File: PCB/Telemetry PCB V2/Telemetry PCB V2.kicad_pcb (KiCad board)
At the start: 4 copper layers, 70 x 70 mm, 44 parts, among them IC1 E22-900M22S, J1 USB_C_Receptacle_USB2.0_16P, J2 Batt, J3 Serial Debug Header 1x4, J4 GPS, J5 Conn_01x04_Pin, SW1 SW_MEC_5E, SW2 SW_MEC_5E, U1 AP62200WU, U2 STM32F411CEUx, U3 MCP1700x-250xxTT, Y1 25MHZ 20pF, Y2 32.768k 12.5pF

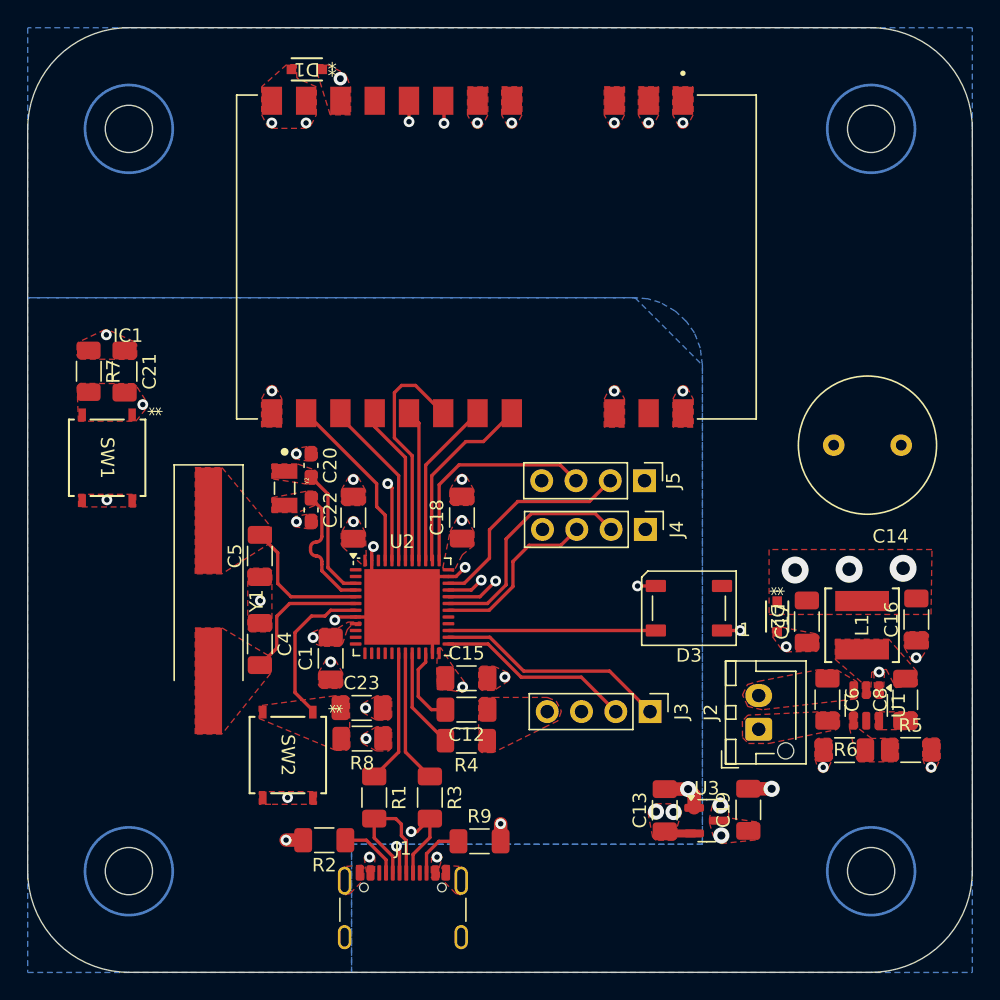
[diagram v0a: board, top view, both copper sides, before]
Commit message: Changed lines around holes to ruled zones
the lines that were used to prevent fills were becoming traces so I changed them to rule zones that prevent anything from entering the zone
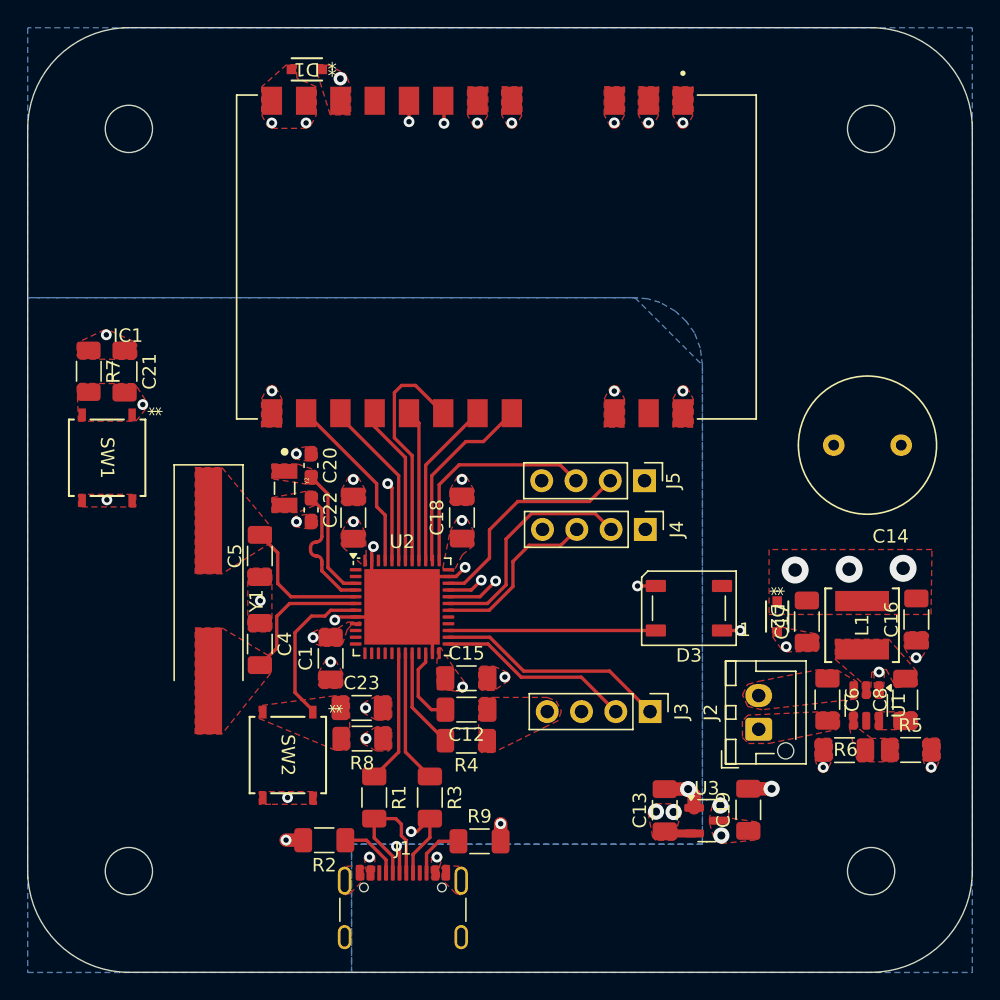
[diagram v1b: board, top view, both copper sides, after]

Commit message: changed many things
changed capacitor footprint, moved tx2 and rx2 to a uart pin. moved nrst switch moved j3 header
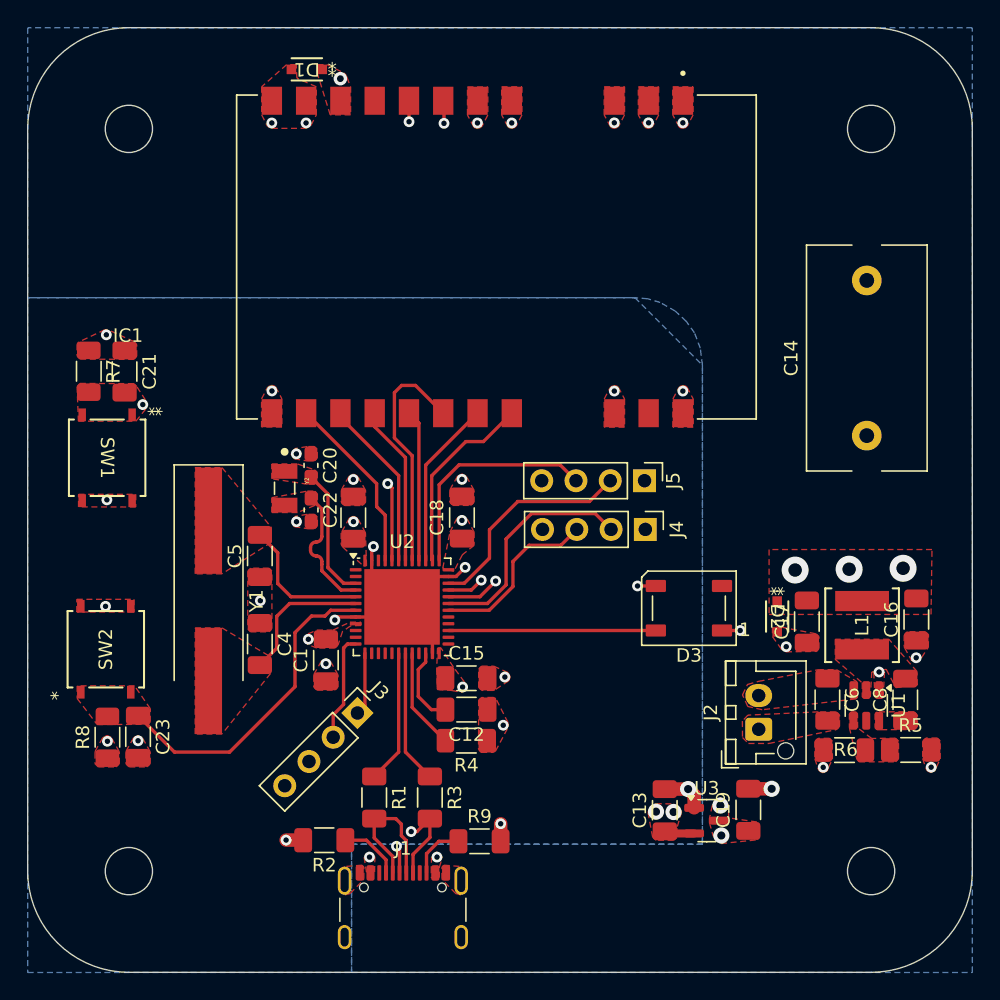
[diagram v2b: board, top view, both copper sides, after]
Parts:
- C14: footprint Capacitor_THT:C_Radial_D10.0mm_H20.0mm_P5.00mm -> PLZ5V1C_G3_H:C_Rect_L16.5mm_W8.7mm_P11.50mm_MKT
- moved J3 21.7 mm to (147.3, 99.2), turned to -45 degrees
- moved R8 18.9 mm to (128.8, 101.0), turned to 90 degrees
- moved C23 16.7 mm to (131.1, 101.0), turned to -90 degrees
- moved SW2 15.6 mm to (128.7, 94.5), turned to 90 degrees
- moved C14 2.76 mm to (185.1, 80.4), turned to 90 degrees
- moved C1 0.37 mm to (145.0, 95.3)
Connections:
- U2 pad 12: unconnected-(U2-PA2-Pad12) -> TX2
- U2 pad 13: unconnected-(U2-PA3-Pad13) -> RX2
- U2 pad 25: TX2 -> unconnected-(U2-PB12-Pad25)
- U2 pad 26: RX2 -> unconnected-(U2-PB13-Pad26)
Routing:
- net RX2: track 17.2 -> 4.66 mm
- net NRST: track 11.6 -> 23.9 mm
- net TX2: track 14.5 -> 7.95 mm
- net GND: vias 32 -> 33

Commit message: Revamped power, made usb better
Revamped the layout of the voltage regulator to match closer to the recommend layout form the data sheet.
Realized I didn't need vias for the usb lines so they are much nicer now
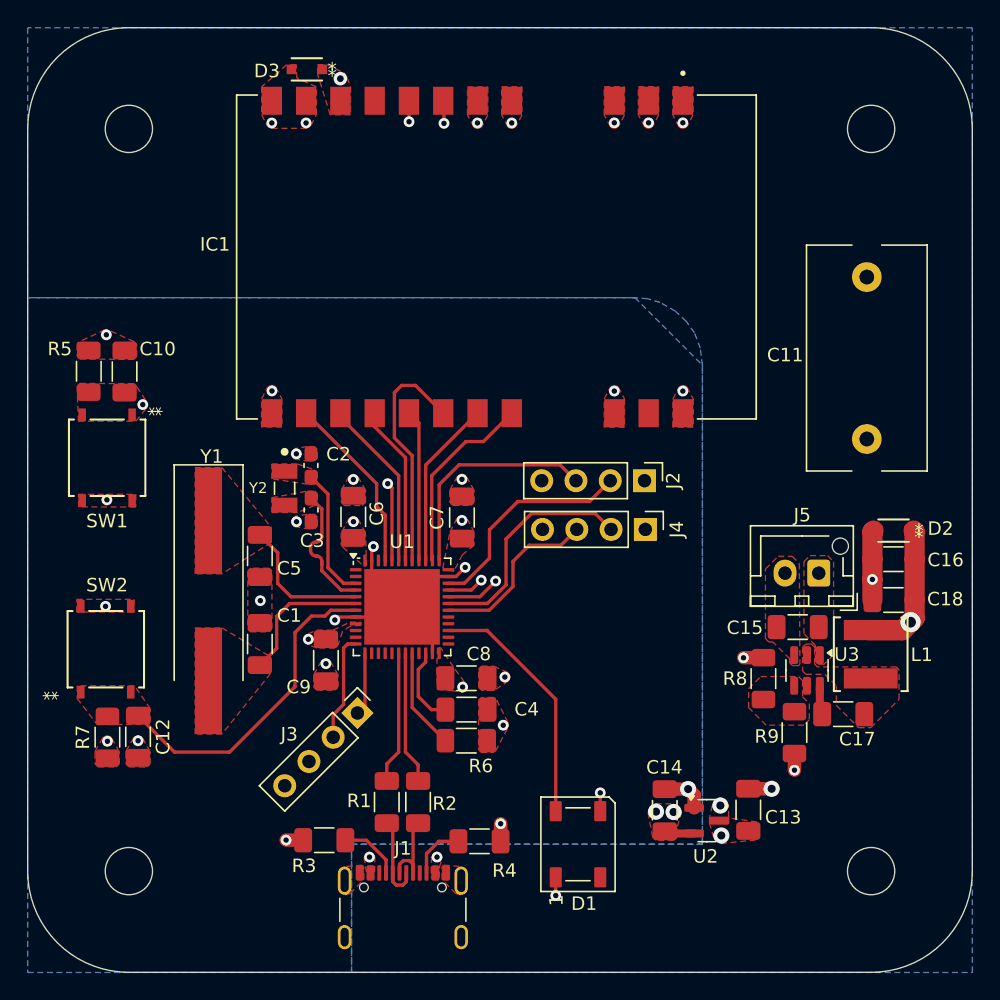
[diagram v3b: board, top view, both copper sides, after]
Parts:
- removed the C11 at (147.0, 84.8)
- added C6: 0.1uF, Capacitor_SMD:C_1206_3216Metric_Pad1.33x1.80mm_HandSolder, F.Cu at (147.0, 84.7)
- C11: renamed from C14; footprint PLZ5V1C_G3_H:C_Rect_L16.5mm_W8.7mm_P11.50mm_MKT -> Custom Capacitor:C_Rect_L16.5mm_W8.7mm_P12.00mm_MKT
- moved D1 19.3 mm to (163.7, 109.0), turned to 90 degrees
- moved J5 12.4 mm to (181.5, 88.9), turned to 180 degrees
- moved R8 12.1 mm to (177.4, 96.7), turned to 90 degrees
- moved D2 10.7 mm to (187.0, 85.7), turned to 180 degrees
- moved C16 7.91 mm to (187.0, 87.8), turned to 0 degrees
- moved C15 5.81 mm to (179.9, 92.9), turned to 0 degrees
- moved U3 5.10 mm to (180.6, 96.1)
- moved C17 4.72 mm to (183.3, 99.3), turned to 0 degrees
- moved R9 3.93 mm to (179.7, 100.7), turned to -90 degrees
- moved L1 2.24 mm to (185.3, 94.9)
- moved C18 2.23 mm to (187.0, 90.9), turned to 0 degrees
- moved R1 0.99 mm to (149.5, 105.8)
- moved R2 0.94 mm to (151.8, 105.8)
- renumbered C4 to C1, C21 to C10, C23 to C12, C19 to C13, C13 to C14, C6 to C15, C17 to C16, C8 to C17, C16 to C18, C20 to C2, C22 to C3, C12 to C4, C18 to C7, C15 to C8, C1 to C9, D3 to D1, D1 to D3, J5 to J2, J2 to J5, R3 to R2, R2 to R3, R9 to R4, R7 to R5, R4 to R6, R8 to R7, R5 to R8, R6 to R9, U2 to U1, U3 to U2, U1 to U3
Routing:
- net +5V: track 1.35 -> 12.9 mm, vias 10 -> 8
- net GND: track 30.1 -> 36.8 mm, vias 33 -> 31
- net USB Dn: track 10.5 -> 6.37 mm
- net USB Dp: track 9.94 -> 6.36 mm, vias 2 -> 0
- net DIN: track 15.4 -> 18.4 mm
- net Net-(U3-BST): track 0.00 -> 2.24 mm
- removed copper zone on F.Cu, net Net-(U3-BST)

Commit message: Large Board Update
Changed stack-up order to signal-ground-power-signal2

tweaked constraints for vias and spacing then adjusted components to fit

changed stm decoupling capacitors to smaller better placed footprints.
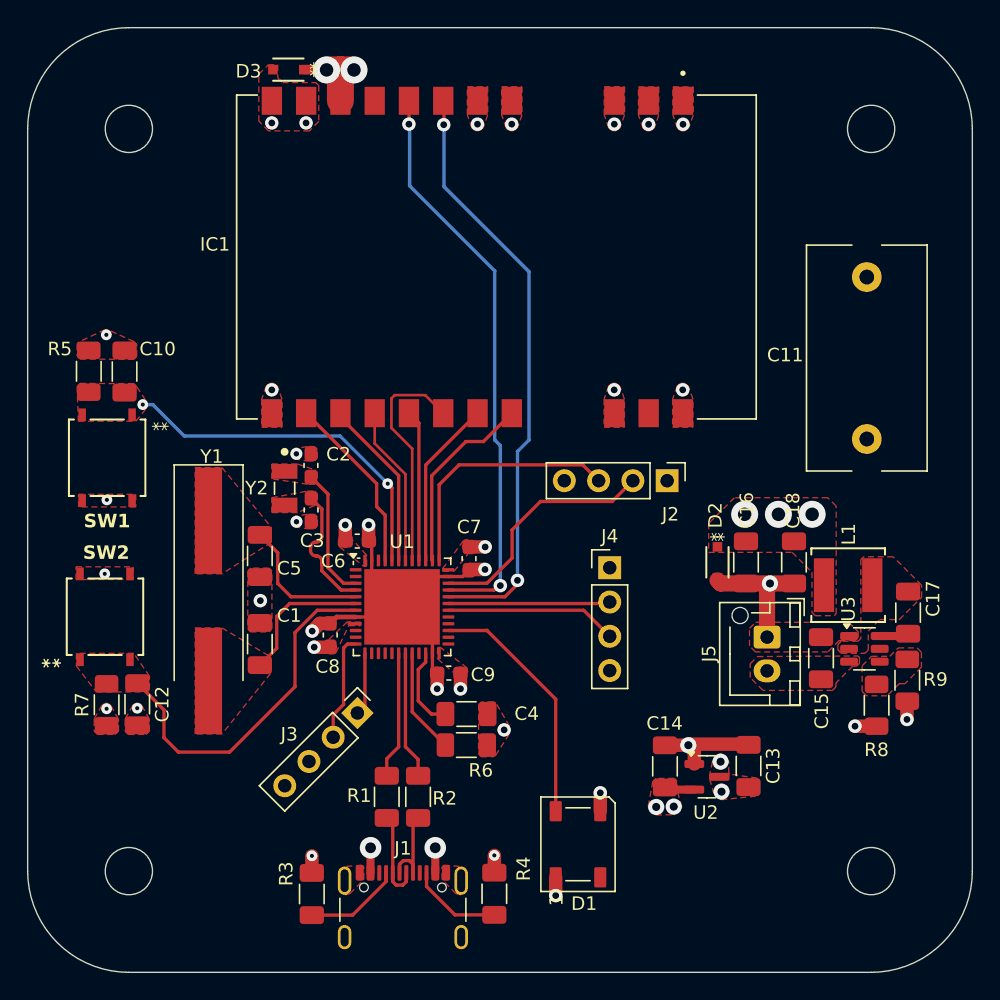
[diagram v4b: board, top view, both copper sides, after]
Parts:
- C6, C7, C8, C9: footprint Capacitor_SMD:C_1206_3216Metric_Pad1.33x1.80mm_HandSolder -> Capacitor_SMD:C_0603_1608Metric_Pad1.08x0.95mm_HandSolder
- J2: value Conn_01x04_Pin -> DBG/PGRM Hdr.
- moved D2 13.3 mm to (174.0, 88.1), turned to -90 degrees
- moved C16 10.9 mm to (176.1, 88.1), turned to 90 degrees
- moved C8 10.6 mm to (145.3, 93.4), turned to 90 degrees
- moved R9 9.21 mm to (188.1, 96.8)
- moved C9 9.16 mm to (154.1, 96.3), turned to 0 degrees
- moved C17 8.93 mm to (188.1, 91.8), turned to 90 degrees
- moved R8 8.61 mm to (185.8, 98.7), turned to -90 degrees
- moved C18 7.89 mm to (179.7, 88.1), turned to 90 degrees
- moved J5 6.10 mm to (177.7, 93.6), turned to -90 degrees
- moved L1 5.38 mm to (183.7, 89.7), turned to 180 degrees
- moved U3 4.54 mm to (184.9, 94.5), turned to 0 degrees
- moved R3 4.09 mm to (143.9, 112.6), turned to 90 degrees
- moved R4 4.04 mm to (157.4, 112.6), turned to 90 degrees
- moved J4 3.88 mm to (166.0, 88.5), turned to 0 degrees
- moved U2 3.25 mm to (173.2, 104.0)
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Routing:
- net GND: track 36.8 -> 52.4 mm, vias 31 -> 27
- net RX: track 17.3 -> 12.0 mm
- net +3.3V: track 2.24 -> 7.50 mm
- net RXEN: track 41.1 -> 44.3 mm
- net Net-(J1-CC2): track 4.17 -> 6.89 mm
- net Net-(J1-CC1): track 4.59 -> 7.17 mm
- net NRST: track 23.9 -> 26.2 mm
- net TXEN: track 40.5 -> 42.7 mm
- net SWDIO: track 16.4 -> 18.0 mm
- net SWCLK: track 16.8 -> 18.5 mm
- net MOSI: track 17.7 -> 17.1 mm
- net +5V: track 12.9 -> 12.5 mm, vias 8 -> 11
- added copper zone on In1.Cu, net +3.3V
- added copper zone on In1.Cu, net +5V
- removed copper zone on B.Cu, net +3.3V
- removed copper zone on B.Cu, net +5V

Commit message: Broad tweaks
Tweaked the location of many power components by small amounts.

Changed to two 1000uF capacitors foe smoothing

swapped Flight computer pin header to 3 pin jst-xh
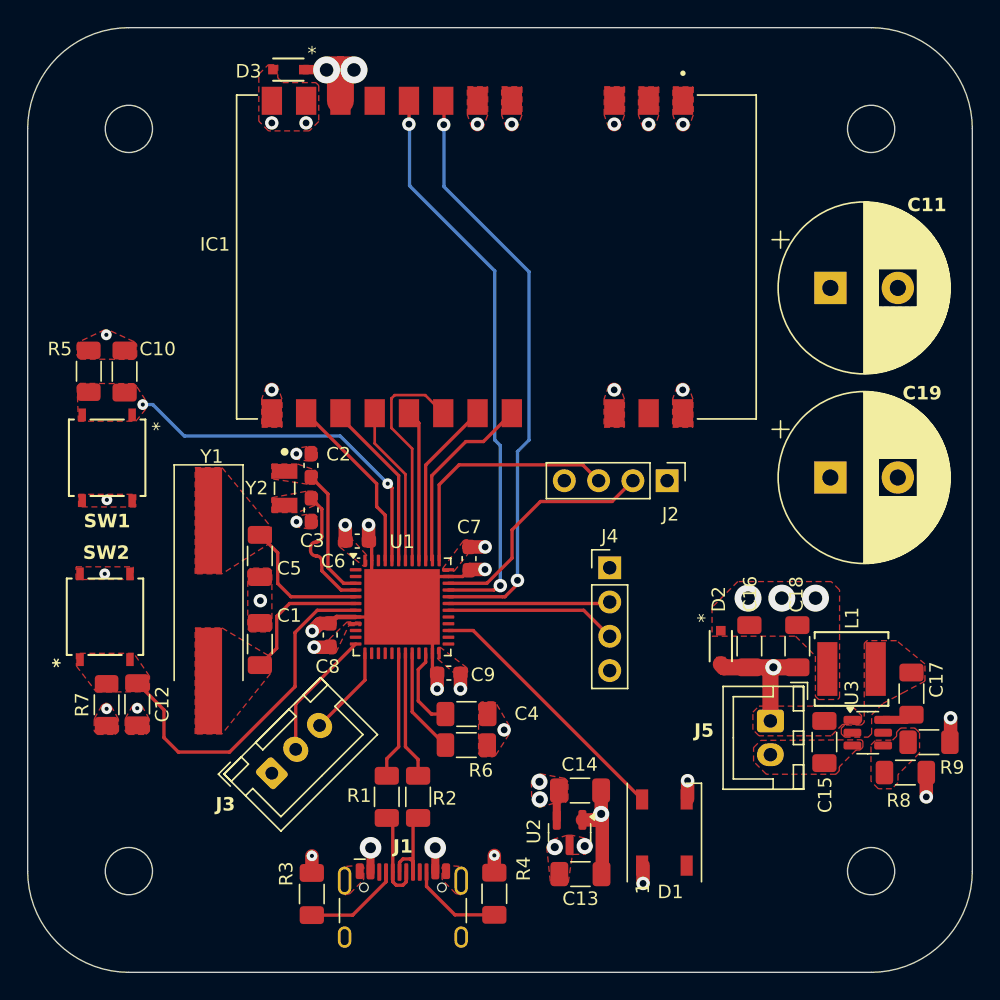
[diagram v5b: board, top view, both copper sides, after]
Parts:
- added C19: 1000uF, Capacitor_THT:CP_Radial_D12.5mm_P5.00mm, F.Cu at (182.3, 81.8)
- C11: value 1F -> 1000uF; footprint Custom Capacitor:C_Rect_L16.5mm_W8.7mm_P12.00mm_MKT -> Capacitor_THT:CP_Radial_D12.5mm_P5.00mm
- J1: footprint Connector_USB:USB_C_Receptacle_GCT_USB4105-xx-A_16P_TopMnt_Horizontal -> Custom Capacitor:USB_C_Receptacle_HCTL_HC-TYPE-C-16P-01A (SMALLER PADS)
- J3: value Serial Debug Header 1x4 -> DATA IN; footprint Connector_PinHeader_2.54mm:PinHeader_1x04_P2.54mm_Vertical -> Connector_JST:JST_XH_B3B-XH-A_1x03_P2.50mm_Vertical
- J5: footprint Connector_JST:JST_XH_B2B-XH-AM_1x02_P2.50mm_Vertical -> Connector_JST:JST_XH_B2B-XH-A_1x02_P2.50mm_Vertical
- moved C13 14.8 mm to (163.8, 111.2), turned to 0 degrees
- moved C11 13.0 mm to (182.3, 67.7), turned to 0 degrees
- moved U2 11.0 mm to (163.0, 108.1), turned to -90 degrees
- moved J3 7.75 mm to (141.0, 103.7), turned to 45 degrees
- moved C14 6.55 mm to (163.8, 105.0), turned to 0 degrees
- moved D1 6.46 mm to (170.1, 108.1)
- moved C16 6.22 mm to (176.3, 94.3)
- moved C18 6.22 mm to (179.9, 94.3)
- moved L1 6.22 mm to (183.9, 96.0)
- moved U3 6.22 mm to (185.1, 100.7)
- moved C15 6.22 mm to (181.9, 101.4)
- moved D2 6.22 mm to (174.2, 94.3)
- moved J5 6.22 mm to (177.9, 99.8)
- moved C17 6.01 mm to (188.4, 97.8)
- moved R8 5.42 mm to (187.9, 103.6), turned to 0 degrees
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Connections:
- J3 pad 1: RX2 -> GND
- J3 pad 3: +3.3V -> RX2
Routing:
- net RX2: track 4.66 -> 6.75 mm
- net TX2: track 7.95 -> 9.65 mm
- net DIN: track 18.4 -> 19.5 mm
- net +5V: track 12.5 -> 13.0 mm
- added copper zone on In2.Cu, net +3.3V
- added copper zone on In2.Cu, net +5V
- added copper zone on In1.Cu, net GND
- removed copper zone on In1.Cu, net +3.3V
- removed copper zone on In1.Cu, net +5V
- removed copper zone on In2.Cu, net GND

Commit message: added test points
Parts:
- added TP1: TestPoint, TestPoint:TestPoint_Loop_D1.80mm_Drill1.0mm_Beaded, F.Cu at (134.3, 62.7)
- added TP2: TestPoint, TestPoint:TestPoint_Loop_D1.80mm_Drill1.0mm_Beaded, F.Cu at (177.9, 114.3)
- added TP3: TestPoint, TestPoint:TestPoint_Loop_D1.80mm_Drill1.0mm_Beaded, F.Cu at (169.1, 101.4)
- added TP4: TestPoint, TestPoint:TestPoint_Loop_D1.80mm_Drill1.0mm_Beaded, F.Cu at (171.2, 114.3)
- added TP5: TestPoint, TestPoint:TestPoint_Loop_D1.80mm_Drill1.0mm_Beaded, F.Cu at (127.8, 62.6)
